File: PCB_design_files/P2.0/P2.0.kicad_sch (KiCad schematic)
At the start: 58 parts, among them J1 EEG_IN, J2 20021121-00008C4LF, U1 INA819IDRGR, U2 TLV9102, U3 TPS61094, U4 TPS60400, U5 NRF52832-QFAA-R, Y1 32MHz

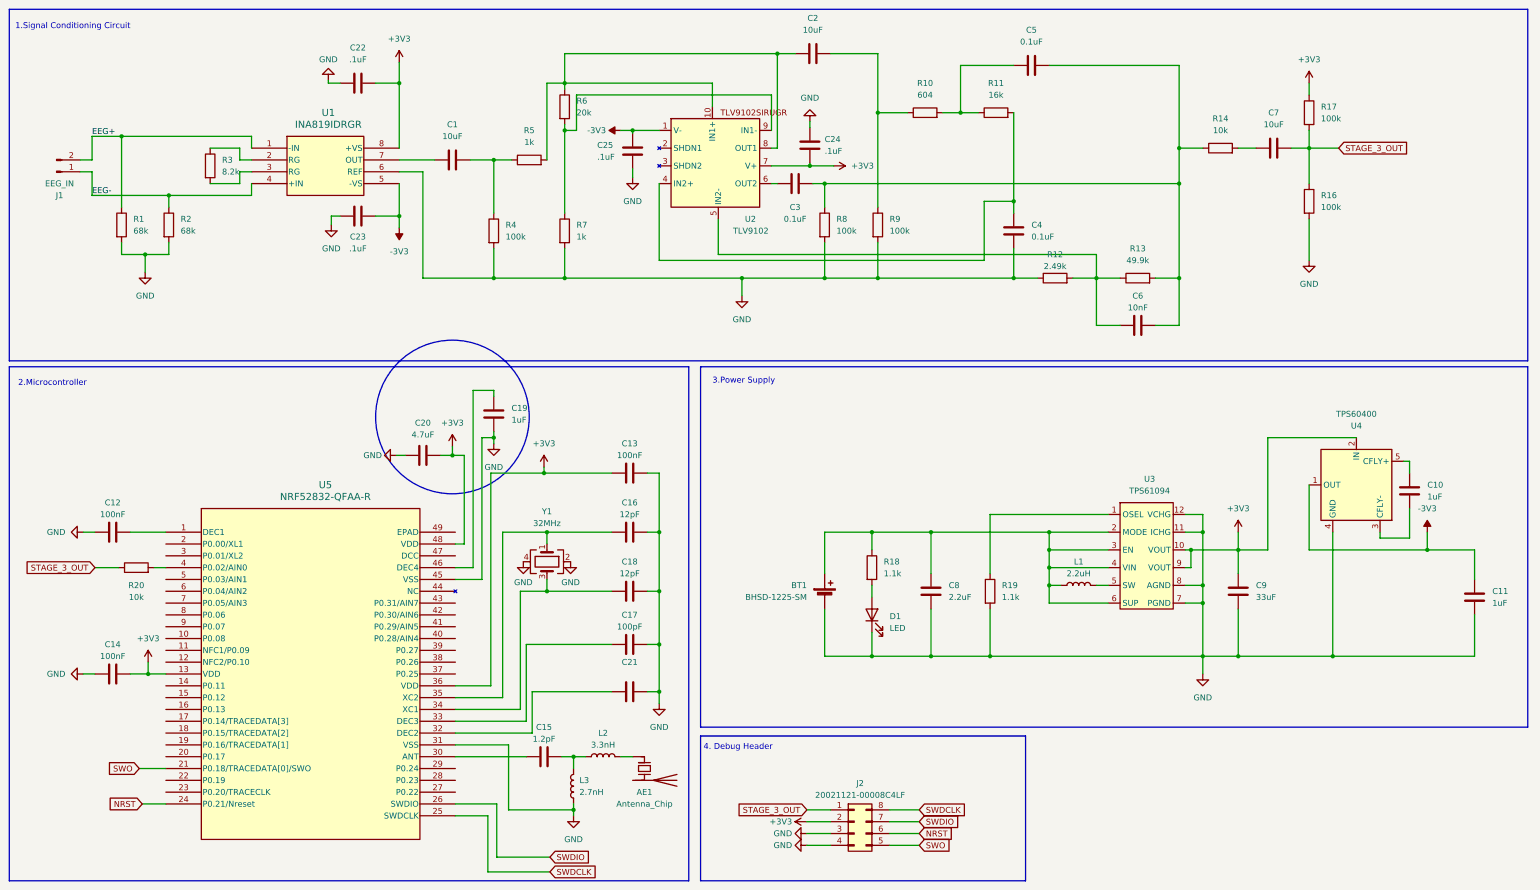
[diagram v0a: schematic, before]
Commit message: Finished assignment of footprints and descriptions
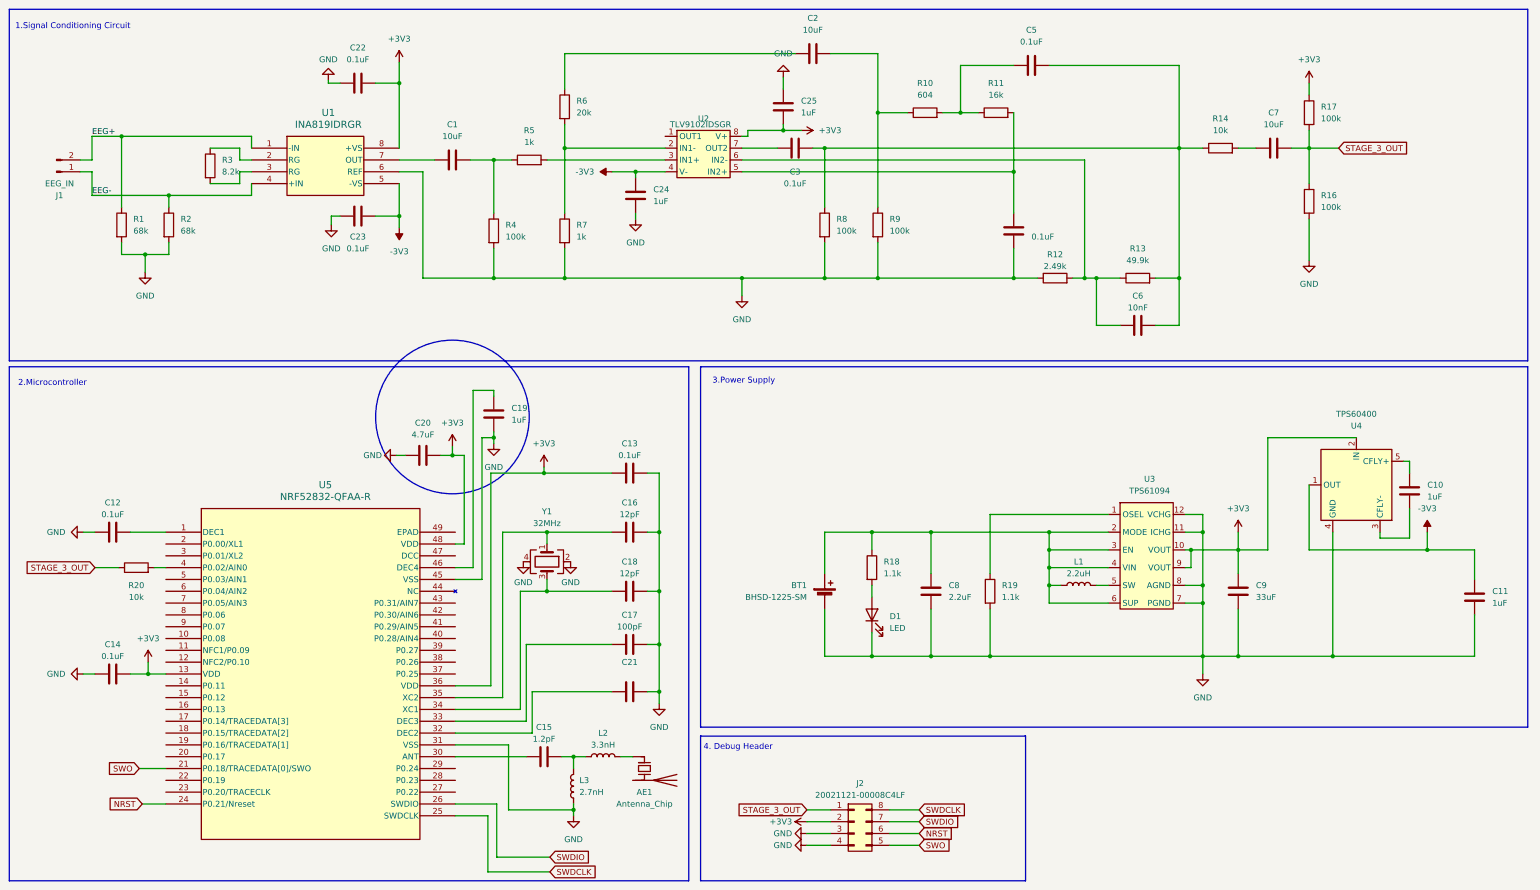
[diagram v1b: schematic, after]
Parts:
- removed U2: TLV9102, Package_DFN_QFN:Texas_R-PUQFN-N10, symbol TLV9102SIRUGR:TLV9102
- added U2: TLV9102IDSGR, Package_SON:WSON-8-1EP_2x2mm_P0.5mm_EP0.9x1.6mm, symbol My_Library:TLV9102
- C1, C2, C7: Manufacturer (none) -> YAGEO; Part Number (none) -> CC0402MPX5R5BB106
- C10, C11: Manufacturer (none) -> TDK Corporation; Part Number (none) -> C1005X5R1E105K050BC
- C12, C13, C14: value 100nF -> 0.1uF; Manufacturer (none) -> TDK Corporation; Part Number (none) -> C1005X7R1C104K050BC
- C15: Manufacturer (none) -> YAGEO; Part Number (none) -> CC0402BRNPO9BN1R2
- C16, C18: Manufacturer (none) -> TDK Corporation; Part Number (none) -> CGA2B2C0G1H120J050BA
- C17: Manufacturer (none) -> TDK Corporation; Part Number (none) -> CGA2B2C0G1H101J050BA
- C19: Manufacturer (none) -> TDK Corporation; Part Number (none) -> C1608X5R1A105K080AC
- C20: Manufacturer (none) -> TDK Corporation; Part Number (none) -> C1608X5R1E475K080AC
- C22, C23: value .1uF -> 0.1uF; Manufacturer (none) -> TDK Corporation; Part Number (none) -> C1005X7R1C104K050BC
- C24, C25: value .1uF -> 1uF; Manufacturer (none) -> TDK Corporation; Part Number (none) -> C1005X5R1E105K050BC
- C3, C4, C5: Manufacturer (none) -> TDK Corporation; Part Number (none) -> C1005X7R1C104K050BC
- C6: Manufacturer (none) -> TDK Corporation; Part Number (none) -> CGA2B2X7R1E103K050BA
- C8: Manufacturer (none) -> TDK Corporation; Part Number (none) -> C1005X5R0J225K050BC
- C9: Manufacturer (none) -> TDK Corporation; Part Number (none) -> C2012X5R0J336M125AC
- L1: footprint Inductor_SMD:L_Murata_DFE201610P -> Inductor_SMD:L_0603_1608Metric; Manufacturer (none) -> Taiyo Yuden; Part Number (none) -> MBKK1608T2R2M
- L2: footprint Inductor_SMD:L_Murata_DFE201610P -> Inductor_SMD:L_0402_1005Metric; Manufacturer (none) -> TDK Corporation; Part Number (none) -> MLG1005S3N3BT000
- L3: footprint Inductor_SMD:L_Murata_DFE201610P -> Inductor_SMD:L_0402_1005Metric; Manufacturer (none) -> TDK Corporation; Part Number (none) -> MLG1005S2N7ST000
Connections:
- net +3V3: now also C25.2, U2.8 (V+); no longer C24.1
- net -3V3: now also C24.2, U2.4 (V-); no longer C25.2
- net GND: now also C24.1; no longer C24.2
- net at C6.1, R12.2, R13.1: now also U2.6 (IN2-)
- net at C2.1, R6.1: no longer R5.2
- net at R6.2, R7.1: now also U2.2 (IN1-)
- net at C4.2, R11.2: now also U2.5 (IN2+)
- net at C3.1: now also U2.7 (OUT2)
- new net: R5.2, U2.3 (IN1+)
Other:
- moved on the sheet: C3

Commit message: Some more revisions
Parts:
- R19: value 1.1k -> 4.75k; Part Number RMCF0402FT1K10 -> RMCF0402FT4K75
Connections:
- net at U2.1 (OUT1): now also C2.1, R6.1
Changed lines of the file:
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@@
   (junction (at 129.54 138.43) (diameter 0) (color 0 0 0 0)
   )
+  (junction (at 147.32 22.86) (diameter 0) (color 0 0 0 0)
+  )
   (junction (at 200.66 71.12) (diameter 0) (color 0 0 0 0)
   )
@@
     (stroke (width 0) (type default))
   )
+  (wire (pts (xy 147.32 22.86) (xy 182.88 22.86))
+    (stroke (width 0) (type default))
+  )
   (wire (pts (xy 270.51 121.92) (xy 270.51 125.73))
     (stroke (width 0) (type default))
   )
+  (wire (pts (xy 154.94 40.64) (xy 147.32 40.64))
+    (stroke (width 0) (type default))
+  )
   (wire (pts (xy 199.39 147.32) (xy 199.39 152.4))
     (stroke (width 0) (type default))
@@
     (stroke (width 0) (type default))
   )
+  (wire (pts (xy 147.32 22.86) (xy 147.32 40.64))
+    (stroke (width 0) (type default))
+  )
   (wire (pts (xy 109.855 184.15) (xy 118.745 184.15))
     (stroke (width 0) (type default))
@@
     (stroke (width 0) (type default))
   )
-  (wire (pts (xy 133.35 22.86) (xy 182.88 22.86))
+  (wire (pts (xy 133.35 22.86) (xy 147.32 22.86))
     (stroke (width 0) (type default))
   )
@@
       (effects (font (size 1.27 1.27)) (justify left))
     )
-    (property "Value" "1.1k" (at 227.33 139.7 0)
+    (property "Value" "4.75k" (at 227.33 139.7 0)
       (effects (font (size 1.27 1.27)) (justify left))
     )
@@
       (effects (font (size 1.27 1.27)) hide)
     )
-    (property "Description" "RES 1.1k OHM 1/16W 1% 0402 SMD" (at 224.79 138.43 0)
+    (property "Description" "RES 4.75k OHM 1/16W 1% 0402 SMD" (at 224.79 138.43 0)
       (effects (font (size 1.27 1.27)) hide)
     )
@@
       (effects (font (size 1.27 1.27)) hide)
     )
-    (property "Part Number" "RMCF0402FT1K10" (at 224.79 138.43 0)
-      (effects (font (size 1.27 1.27)) hide)
-    )
+    (property "Part Number" "RMCF0402FT4K75" (at 224.79 138.43 0)
+      (effects (font (size 1.27 1.27)) hide)
+    )

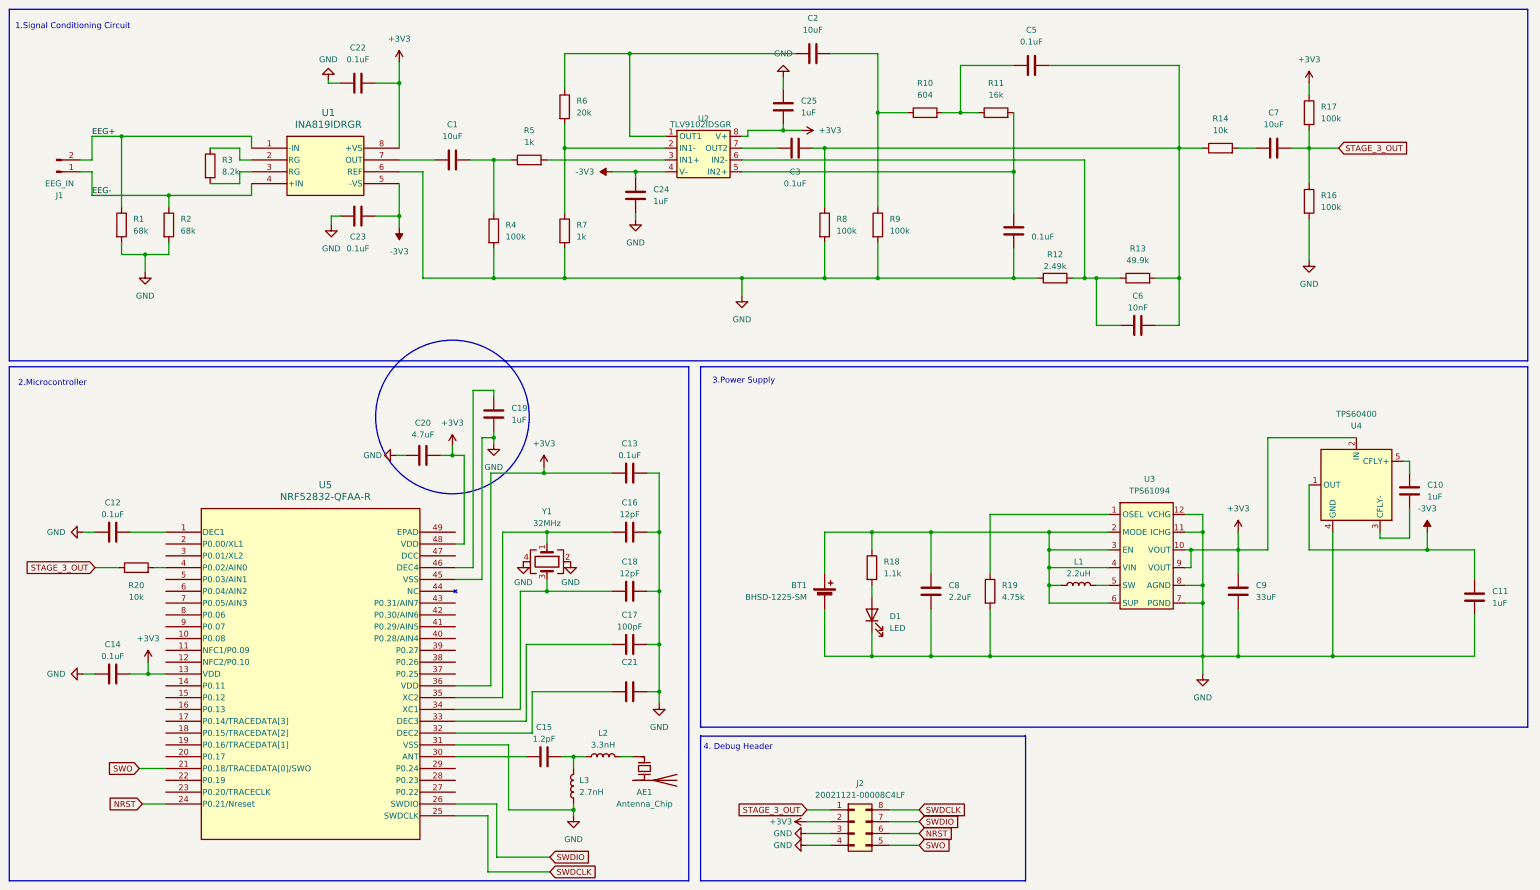
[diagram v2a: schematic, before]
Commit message: made some schematic updates
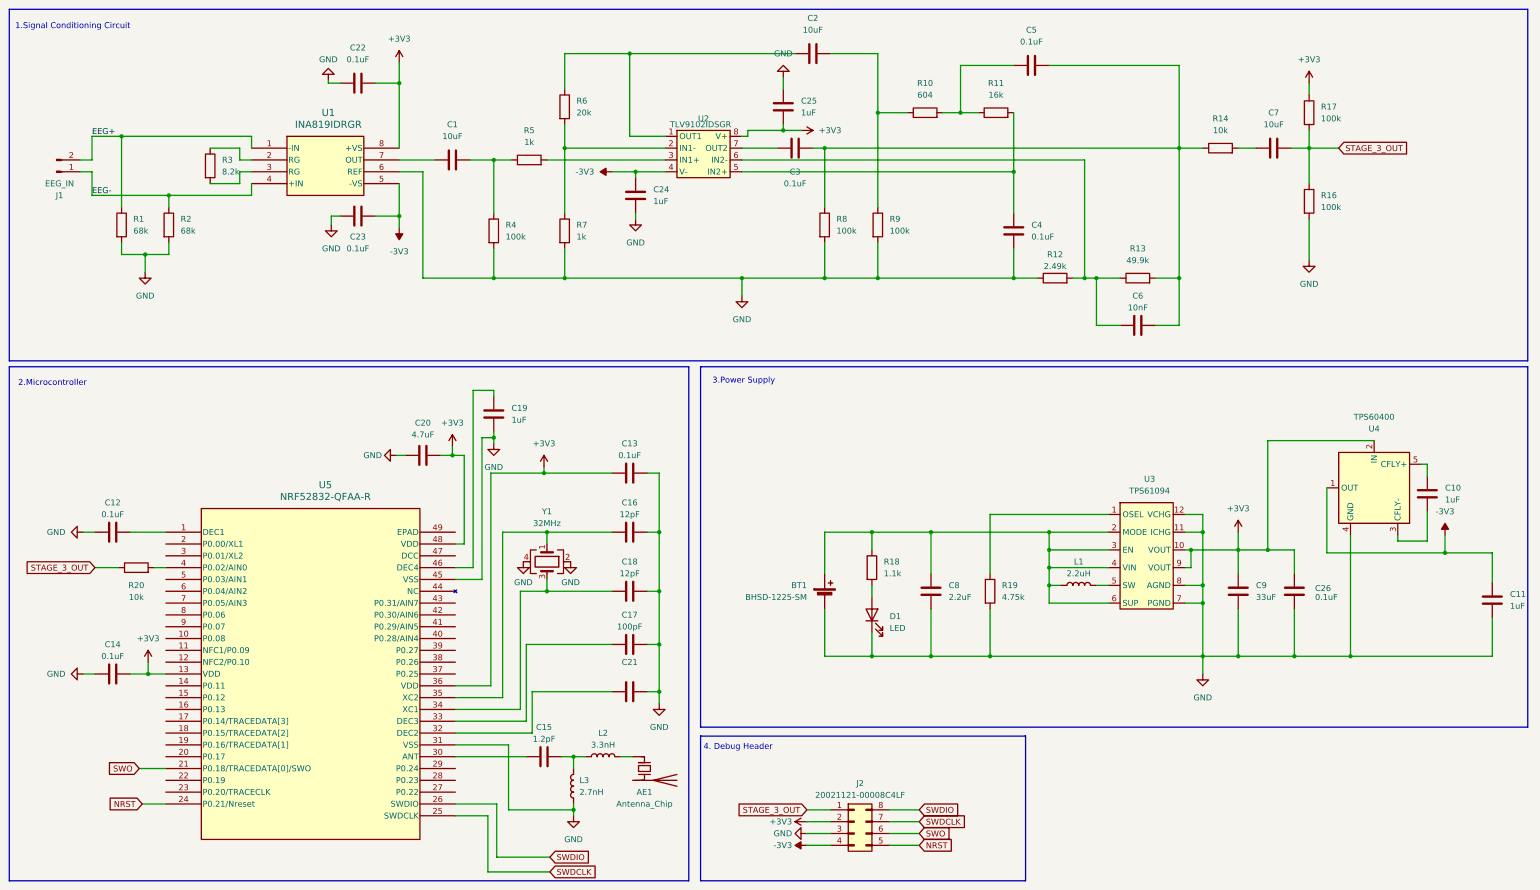
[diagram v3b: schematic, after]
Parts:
- added C26: 0.1uF, Capacitor_SMD:C_0402_1005Metric, symbol Device:C
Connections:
- net +3V3: now also C26.2
- net -3V3: now also J2.4 (Pin_4)
- net GND: now also C26.1; no longer J2.4 (Pin_4)
- net NRST: now also J2.5 (Pin_5); no longer J2.6 (Pin_6)
- net SWDCLK: now also J2.7 (Pin_7); no longer J2.8 (Pin_8)
- net SWDIO: now also J2.8 (Pin_8); no longer J2.7 (Pin_7)
- net SWO: now also J2.6 (Pin_6); no longer J2.5 (Pin_5)
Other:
- moved on the sheet: C10, C11, U4

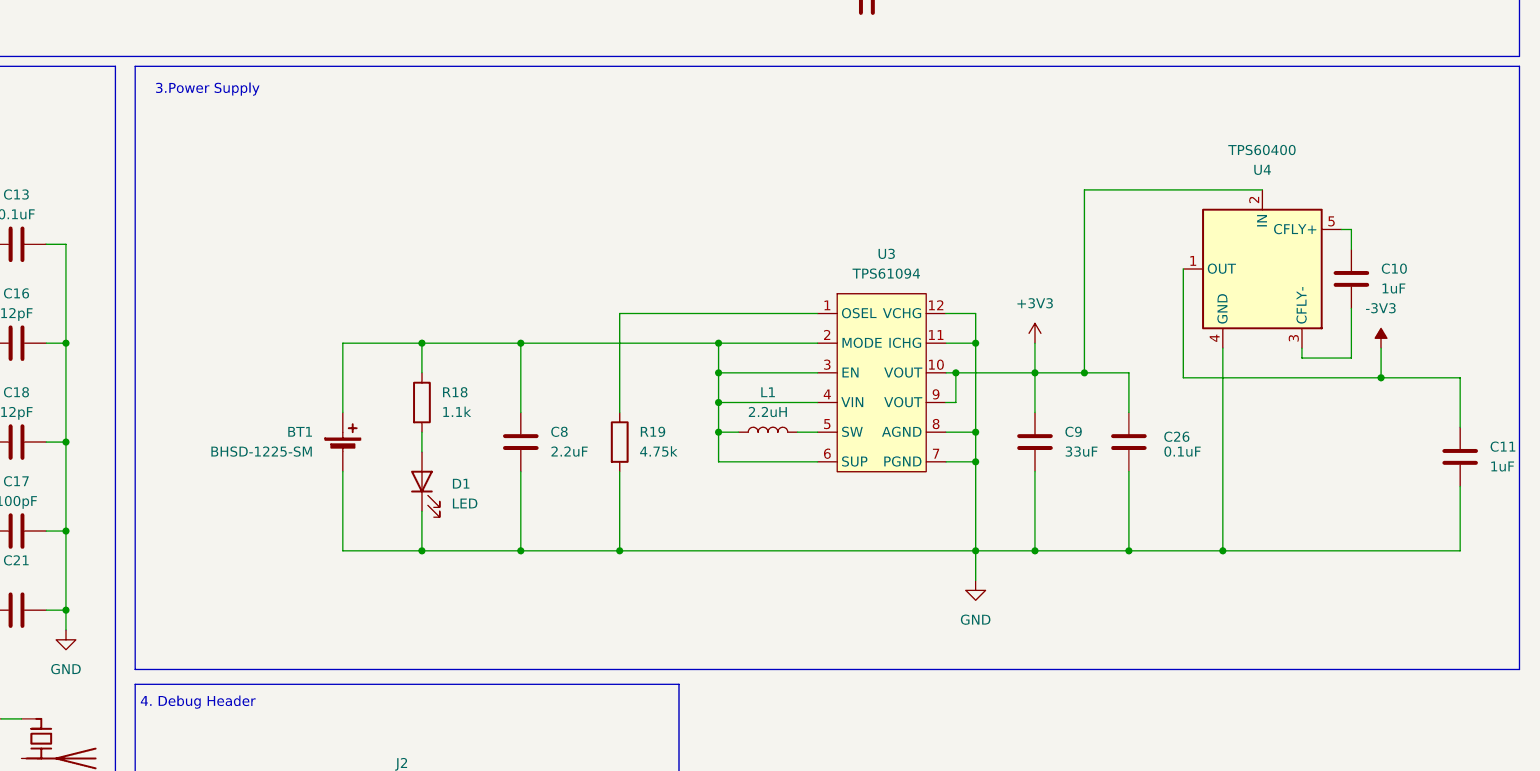
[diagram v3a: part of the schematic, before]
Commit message: Schematic updates
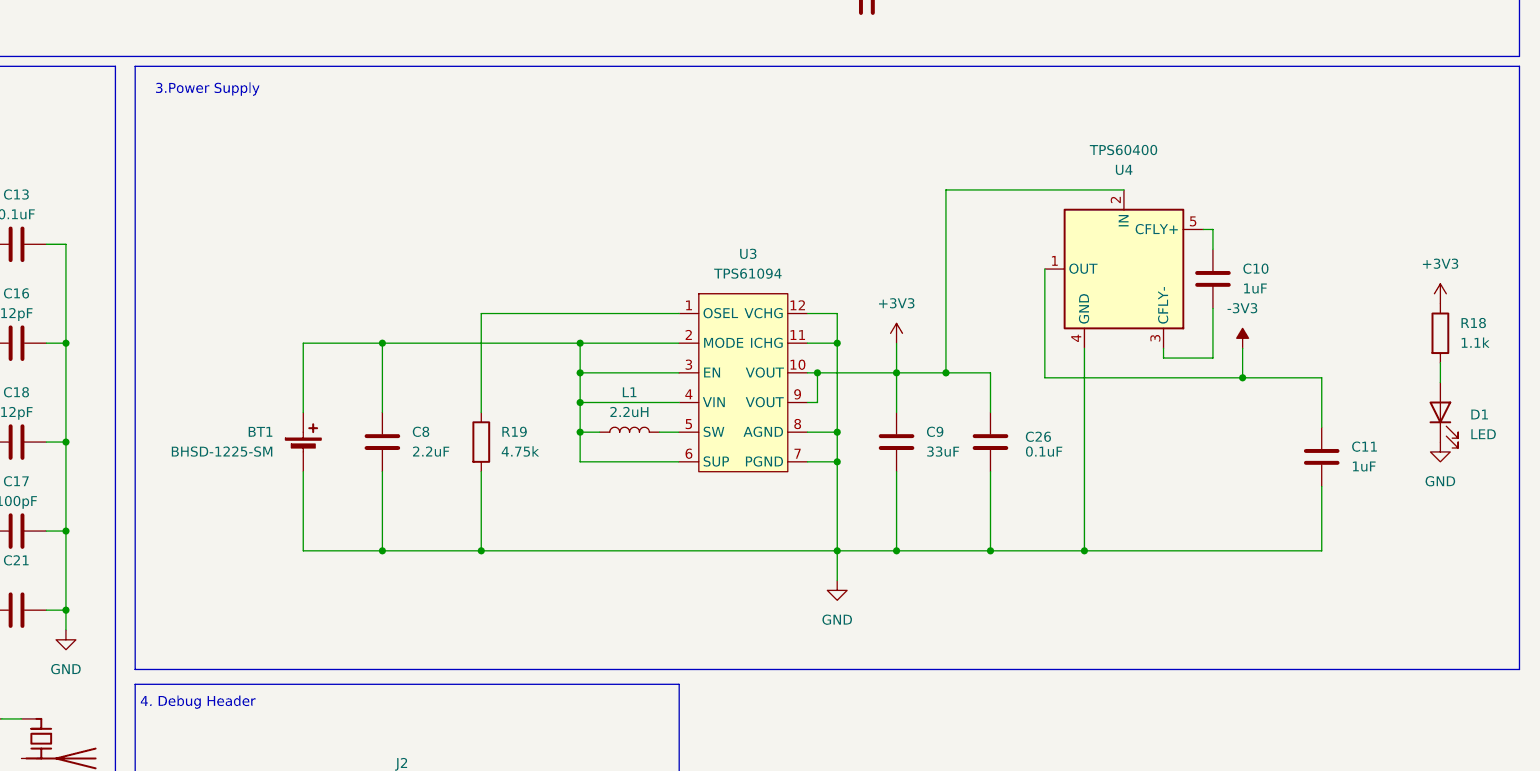
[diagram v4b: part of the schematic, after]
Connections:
- net +3V3: now also R18.1
- net at BT1.1 (+), C8.2, L1.1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: no longer R18.1
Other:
- moved on the sheet: BT1, C10, C11, C26, C8, C9, D1, L1, R18, R19, U3, U4

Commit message: Updated schematic
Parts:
- removed C21: ~, Capacitor_SMD:C_0402_1005Metric, symbol Device:C
- removed J2: 20021121-00008C4LF, 20021121_00008C4LF:AMPHENOL_20021121-00008C4LF, symbol Connector_Generic:Conn_02x04_Counter_Clockwise
- added J2: Conn_02x03_Counter_Clockwise, 20021121_00006C4LF:AMPHENOL_20021121-00006C4LF, symbol Connector_Generic:Conn_02x03_Counter_Clockwise
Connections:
- net +3V3: now also J2.2 (Pin_2)
- net -3V3: now also J2.1 (Pin_1)
- net GND: now also J2.6 (Pin_6)
- net STAGE_3_OUT: now also J2.3 (Pin_3)
- net SWDCLK: now also J2.5 (Pin_5)
- net SWDIO: now also J2.4 (Pin_4)
- net NRST: no longer names the net of U5.24 (P0.21/Nreset)
- net SWO: no longer names the net of U5.21 (P0.18/TRACEDATA[0]/SWO)
